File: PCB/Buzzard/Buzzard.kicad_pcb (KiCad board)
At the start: 2 copper layers, 151.7 x 93.9 mm, 87 parts, among them J2 LCD, J4 Haptic Buzz, J5 TrackPoint, J6 OLED, J8 Battery, SW1 SW_DPST_x2, U1 ProMicro, U10 Hole, U11 Hole, U12 Hole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

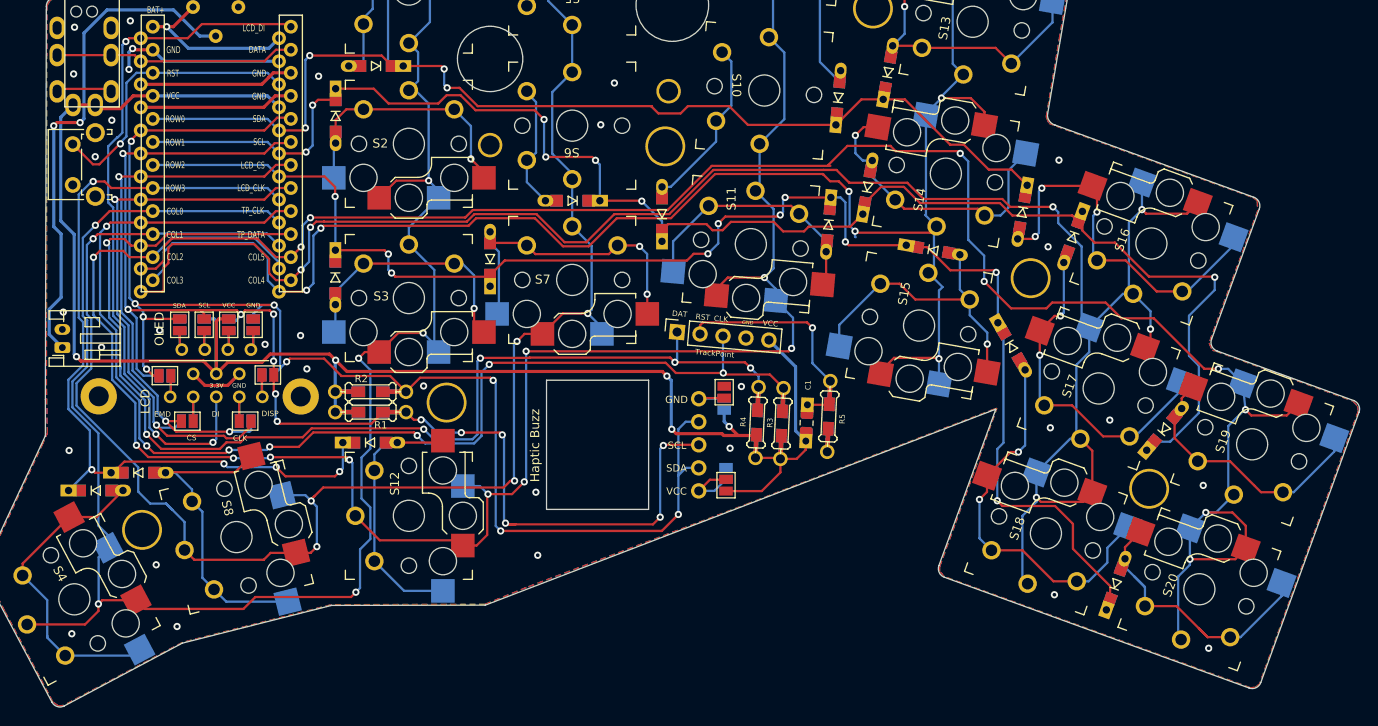
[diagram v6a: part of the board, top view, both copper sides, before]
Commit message: moved pinky column more to the middle
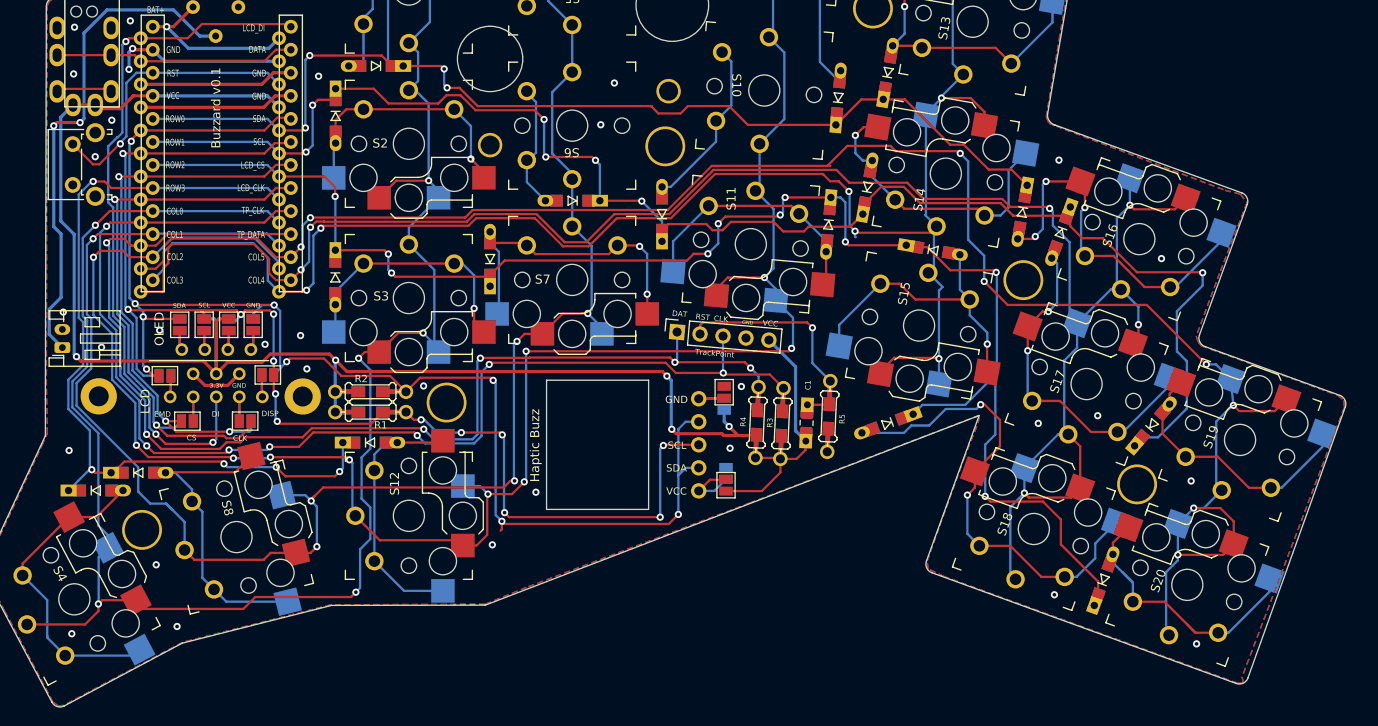
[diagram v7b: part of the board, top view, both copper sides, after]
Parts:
- moved D18 16.1 mm to (177.3, 100.0), turned to -160 degrees
- moved D20 1.42 mm to (201.1, 117.2)
- moved S17 1.42 mm to (199.2, 95.6)
- moved S19 1.42 mm to (216.1, 101.8)
- moved U4 1.42 mm to (204.8, 106.7)
- moved S18 1.42 mm to (193.4, 111.6)
- moved S20 1.42 mm to (210.3, 117.8)
- moved D17 1.42 mm to (196.4, 78.9)
- moved D19 1.42 mm to (206.4, 100.1)
- moved S16 1.42 mm to (205.0, 79.7)
- moved U7 0.83 mm to (192.2, 84.2)
- moved U3 0.22 mm to (112.8, 97.0)
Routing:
- net ROW2: track 157.4 -> 169.3 mm
- net Net-(D18-Pad2): track 42.9 -> 53.0 mm
- net SCL: track 142.6 -> 140.2 mm
- net COL4: track 213.8 -> 211.7 mm
- net COL5: track 202.8 -> 200.8 mm
- net Net-(D16-Pad2): track 41.9 -> 39.9 mm
- net ROW1: track 166.2 -> 164.7 mm
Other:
- board size 151.7 x 93.9 mm -> 150.2 x 93.9 mm
- board text added: "Buzzard v0.1"

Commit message: adding logo
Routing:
- net SDA: track 155.4 -> 154.0 mm
- net SCL: track 140.2 -> 139.6 mm
